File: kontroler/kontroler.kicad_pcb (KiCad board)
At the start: 2 copper layers, 147 x 78 mm, 44 parts, among them IC1 ATTINY841-SSU, P1 CONN_01X01, P2 CONN_01X01, P3 CONN_01X01, P4 CONN_01X01, P5 CONN_01X06, P6 CONN_01X06, P7 CONN_01X06, Q1 Q_PMOS_GDSD, Q2 Q_NPN_BEC, Q3 IRF8721PBF-1, Q4 Q_NMOS_GDSD, Q5 Q_NMOS_GDSD, Q6 Q_NMOS_GDSD, SW1 SW_PUSH, SW2 SW_PUSH, SW3 SW_PUSH, SW4 SW_PUSH, U1 LD1117S50CTR

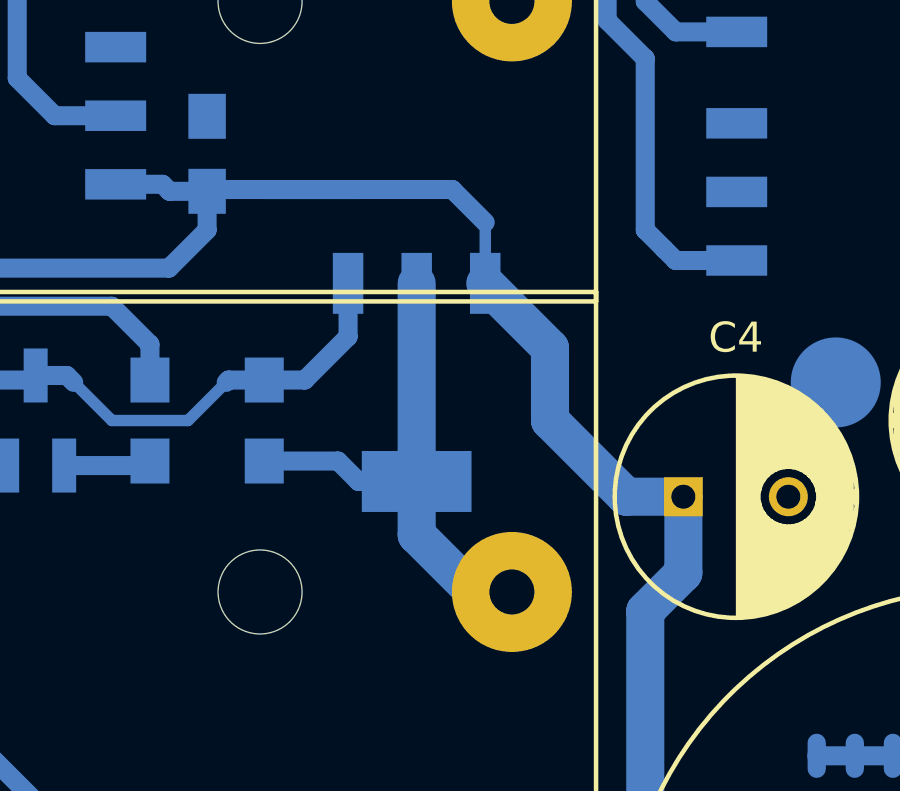
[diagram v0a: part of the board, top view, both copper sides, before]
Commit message: Fixed wrong p-mos orientation
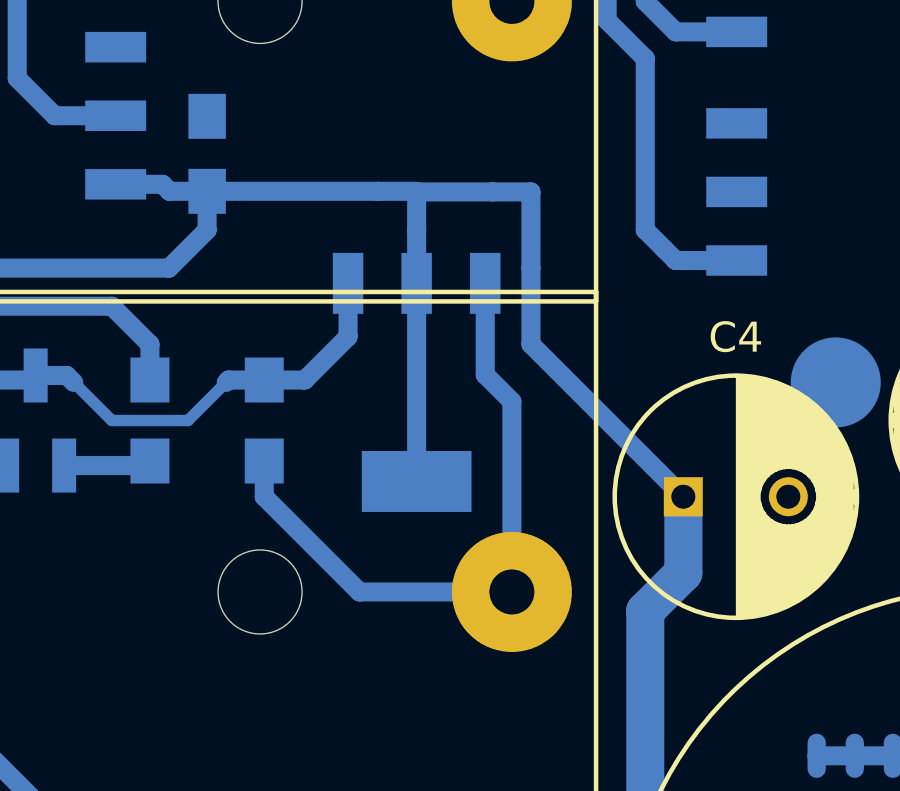
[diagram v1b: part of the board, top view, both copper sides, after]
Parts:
- R2: value R -> 33k
- R3: value R -> 12k
- R5: value R -> 47k
- R6: value R -> 3k3
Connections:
- Q1 pad 2: Net-(BT1-Pad1) -> Net-(C1-Pad1)
- Q1 pad 3: Net-(C1-Pad1) -> Net-(BT1-Pad1)
- Q1 pad 4: Net-(BT1-Pad1) -> Net-(C1-Pad1)
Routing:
- net Net-(BT1-Pad1): track 17.7 -> 22.7 mm
- net Net-(C1-Pad1): track 74.0 -> 69.1 mm

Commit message: Better layout
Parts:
- moved Q1 1.27 mm to (114.3, 74.9), turned to 180 degrees
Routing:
- net Net-(C1-Pad1): track 69.1 -> 58.2 mm
- net Net-(BT1-Pad1): track 22.7 -> 13.6 mm
- net Net-(D2-Pad2): track 18.2 -> 23.5 mm
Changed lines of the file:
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@@
   (general
     (links 94)
-    (no_connects 3)
+    (no_connects 4)
     (area 31.924999 39.924999 179.075001 118.075001)
     (thickness 1.6)
     (drawings 12)
-    (tracks 250)
+    (tracks 249)
     (zones 0)
     (modules 44)
@@
   )
   (module TO_SOT_Packages_SMD:SOT-223 (layer B.Cu)
-    (at 114.3 76.2)
+    (at 114.3 74.93 180)
     (descr "module CMS SOT223 4 pins")
     (tags "CMS SOT")
     (attr smd)
-    (fp_text reference Q1 (at 0 0.762) (layer B.SilkS)
-      (effects (font (size 1 1) (thickness 0.15)) (justify mirror))
-    )
-    (fp_text value Q_PMOS_GDSD (at 0 -0.762) (layer B.Fab)
+    (fp_text reference Q1 (at 0 0.762 180) (layer B.SilkS)
+      (effects (font (size 1 1) (thickness 0.15)) (justify mirror))
+    )
+    (fp_text value Q_PMOS_GDSD (at 0 -0.762 180) (layer B.Fab)
       (effects (font (size 1 1) (thickness 0.15)) (justify mirror))
     )
@@
     (fp_line (start 2.032 4.572) (end 3.556 2.286) (layer B.SilkS) (width 0.15))
     (fp_line (start 3.556 2.286) (end 3.556 1.524) (layer B.SilkS) (width 0.15))
-    (pad 4 smd rect (at 0 3.302) (size 3.6576 2.032) (layers B.Cu B.Paste B.Mask)
+    (pad 4 smd rect (at 0 3.302 180) (size 3.6576 2.032) (layers B.Cu B.Paste B.Mask)
       (net 4 "Net-(C1-Pad1)"))
-    (pad 2 smd rect (at 0 -3.302) (size 1.016 2.032) (layers B.Cu B.Paste B.Mask)
+    (pad 2 smd rect (at 0 -3.302 180) (size 1.016 2.032) (layers B.Cu B.Paste B.Mask)
       (net 4 "Net-(C1-Pad1)"))
-    (pad 3 smd rect (at 2.286 -3.302) (size 1.016 2.032) (layers B.Cu B.Paste B.Mask)
+    (pad 3 smd rect (at 2.286 -3.302 180) (size 1.016 2.032) (layers B.Cu B.Paste B.Mask)
       (net 1 "Net-(BT1-Pad1)"))
-    (pad 1 smd rect (at -2.286 -3.302) (size 1.016 2.032) (layers B.Cu B.Paste B.Mask)
+    (pad 1 smd rect (at -2.286 -3.302 180) (size 1.016 2.032) (layers B.Cu B.Paste B.Mask)
       (net 10 "Net-(D2-Pad2)"))
     (model TO_SOT_Packages_SMD.3dshapes/SOT-223.wrl
@@
   (gr_line (start 156 118) (end 156 40) (angle 90) (layer Edge.Cuts) (width 0.15))
   (gr_line (start 32 118) (end 156 118) (angle 90) (layer Edge.Cuts) (width 0.15))
-  (segment (start 117.475 83.185) (end 117.475 76.835) (width 0.635) (layer B.Cu) (net 1) (status 400000))
-  (segment (start 116.586 75.946) (end 116.586 72.898) (width 0.635) (layer B.Cu) (net 1) (status 800000))
-  (segment (start 117.475 76.835) (end 116.586 75.946) (width 0.635) (layer B.Cu) (net 1))
-  (segment (start 109.22 78.82) (end 109.22 80.01) (width 0.635) (layer B.Cu) (net 1))
-  (segment (start 112.395 83.185) (end 117.475 83.185) (width 0.635) (layer B.Cu) (net 1))
-  (segment (start 109.22 80.01) (end 112.395 83.185) (width 0.635) (layer B.Cu) (net 1))
+  (segment (start 109.22 78.82) (end 112.014 78.82) (width 0.635) (layer B.Cu) (net 1) (status C00000))
+  (segment (start 112.014 78.82) (end 111.934 78.74) (width 0.635) (layer B.Cu) (net 1) (status C00000))
+  (segment (start 111.934 78.74) (end 111.76 78.74) (width 0.635) (layer B.Cu) (net 1) (status C00000))
+  (segment (start 111.76 78.74) (end 112.014 78.232) (width 0.635) (layer B.Cu) (net 1) (status C00000))
+  (segment (start 117.475 83.185) (end 114.935 83.185) (width 1.27) (layer B.Cu) (net 1) (status 400000))
+  (segment (start 112.014 80.264) (end 112.014 78.232) (width 1.27) (layer B.Cu) (net 1) (status 800000))
+  (segment (start 114.935 83.185) (end 112.014 80.264) (width 1.27) (layer B.Cu) (net 1))
   (segment (start 117.475 83.185) (end 116.205 83.185) (width 1.27) (layer B.Cu) (net 1))
   (segment (start 45.085 83.185) (end 45.085 63.5) (width 2.54) (layer B.Cu) (net 2))
@@
   (segment (start 118.11 97.155) (end 118.11 104.14) (width 0.635) (layer F.Cu) (net 3))
   (via (at 118.11 97.155) (size 1.5) (drill 0.7) (layers F.Cu B.Cu) (net 3))
-  (segment (start 114.3 69.85) (end 116.84 69.85) (width 0.635) (layer B.Cu) (net 4))
-  (segment (start 118.11 74.93) (end 123.19 80.01) (width 0.635) (layer B.Cu) (net 4) (status 800000))
-  (segment (start 118.11 72.39) (end 118.11 74.93) (width 0.635) (layer B.Cu) (net 4))
-  (segment (start 118.11 69.85) (end 118.11 72.39) (width 0.635) (layer B.Cu) (net 4))
-  (segment (start 116.84 69.85) (end 118.11 69.85) (width 0.635) (layer B.Cu) (net 4))
-  (segment (start 114.3 71.12) (end 114.3 69.85) (width 0.635) (layer B.Cu) (net 4))
-  (segment (start 114.3 72.898) (end 114.3 71.12) (width 0.635) (layer B.Cu) (net 4) (status 400000))
-  (segment (start 114.28 69.83) (end 113.03 69.83) (width 0.635) (layer B.Cu) (net 4))
-  (segment (start 114.3 69.85) (end 114.28 69.83) (width 0.635) (layer B.Cu) (net 4))
-  (segment (start 107.315 69.83) (end 113.03 69.83) (width 0.635) (layer B.Cu) (net 4) (status 400000))
+  (segment (start 114.3 71.628) (end 117.348 71.628) (width 1.27) (layer B.Cu) (net 4) (status 400000))
+  (segment (start 119.38 76.2) (end 123.19 80.01) (width 1.27) (layer B.Cu) (net 4) (status 800000))
+  (segment (start 119.38 73.66) (end 119.38 76.2) (width 1.27) (layer B.Cu) (net 4))
+  (segment (start 117.348 71.628) (end 119.38 73.66) (width 1.27) (layer B.Cu) (net 4))
+  (segment (start 113.03 69.83) (end 113.03 69.85) (width 0.635) (layer B.Cu) (net 4))
+  (segment (start 113.03 69.85) (end 114.3 71.12) (width 0.635) (layer B.Cu) (net 4) (status 800000))
+  (segment (start 114.3 71.12) (end 114.3 71.628) (width 0.635) (layer B.Cu) (net 4) (status C00000))
+  (segment (start 107.315 69.83) (end 113.03 69.83) (width 0.635) (layer B.Cu) (net 4))
   (segment (start 113.03 69.83) (end 113.01 69.83) (width 0.635) (layer B.Cu) (net 4))
-  (segment (start 114.3 79.502) (end 114.3 72.898) (width 0.635) (layer B.Cu) (net 4))
   (segment (start 107.375 69.77) (end 107.315 69.83) (width 0.635) (layer B.Cu) (net 4))
   (segment (start 106.045 72.39) (end 93.345 72.39) (width 0.635) (layer B.Cu) (net 4))
@@
   (segment (start 93.345 72.39) (end 92.394594 71.439594) (width 0.635) (layer B.Cu) (net 4))
   (segment (start 121.92 95.25) (end 121.92 83.82) (width 1.27) (layer B.Cu) (net 4))
+  (segment (start 121.92 83.82) (end 123.19 82.55) (width 1.27) (layer B.Cu) (net 4))
   (segment (start 123.19 82.55) (end 123.19 80.01) (width 1.27) (layer B.Cu) (net 4))
-  (segment (start 121.92 83.82) (end 123.19 82.55) (width 1.27) (layer B.Cu) (net 4))
   (segment (start 107.335 69.85) (end 107.315 69.83) (width 0.381) (layer B.Cu) (net 4))
   (segment (start 107.315 69.83) (end 106.065 69.83) (width 0.635) (layer B.Cu) (net 4))
@@
   (segment (start 84.836 71.882) (end 87.122 71.882) (width 0.381) (layer B.Cu) (net 9))
   (segment (start 84.709 71.755) (end 84.836 71.882) (width 0.381) (layer B.Cu) (net 9))
-  (segment (start 112.014 72.898) (end 112.014 74.676) (width 0.635) (layer B.Cu) (net 10))
-  (segment (start 110.57 76.12) (end 109.22 76.12) (width 0.635) (layer B.Cu) (net 10))
-  (segment (start 112.014 74.676) (end 110.57 76.12) (width 0.635) (layer B.Cu) (net 10))
+  (segment (start 109.22 76.12) (end 109.3 76.12) (width 0.635) (layer B.Cu) (net 10) (status C00000))
+  (segment (start 109.3 76.12) (end 110.49 74.93) (width 0.635) (layer B.Cu) (net 10) (status 400000))
+  (segment (start 116.586 75.946) (end 116.586 78.232) (width 0.635) (layer B.Cu) (net 10) (status 800000))
+  (segment (start 115.57 74.93) (end 116.586 75.946) (width 0.635) (layer B.Cu) (net 10))
+  (segment (start 110.49 74.93) (end 115.57 74.93) (width 0.635) (layer B.Cu) (net 10))
+  (segment (start 109.22 76.12) (end 108.03 76.12) (width 0.635) (layer B.Cu) (net 10) (status 400000))
+  (segment (start 104.14 77.47) (end 102.87 76.2) (width 0.381) (layer B.Cu) (net 10))
+  (segment (start 106.68 77.47) (end 104.14 77.47) (width 0.381) (layer B.Cu) (net 10))
+  (segment (start 102.63886 75.96886) (end 102.87 76.2) (width 0.635) (layer B.Cu) (net 10))
+  (segment (start 102.63886 75.96886) (end 101.6 75.96886) (width 0.635) (layer B.Cu) (net 10))
   (segment (start 108.03 76.12) (end 106.68 77.47) (width 0.381) (layer B.Cu) (net 10))
-  (segment (start 109.22 76.12) (end 108.03 76.12) (width 0.635) (layer B.Cu) (net 10))
-  (segment (start 108.03 76.12) (end 107.95 76.2) (width 0.635) (layer B.Cu) (net 10))
   (segment (start 97.79 76.12) (end 101.44886 76.12) (width 0.635) (layer B.Cu) (net 10))
   (segment (start 101.44886 76.12) (end 101.6 75.96886) (width 0.635) (layer B.Cu) (net 10))
-  (segment (start 101.6 75.96886) (end 102.63886 75.96886) (width 0.635) (layer B.Cu) (net 10))
-  (segment (start 102.63886 75.96886) (end 102.87 76.2) (width 0.635) (layer B.Cu) (net 10))
-  (segment (start 106.68 77.47) (end 104.14 77.47) (width 0.381) (layer B.Cu) (net 10))
-  (segment (start 104.14 77.47) (end 102.87 76.2) (width 0.381) (layer B.Cu) (net 10))
   (segment (start 101.6 76.2) (end 101.6 75.96886) (width 0.381) (layer B.Cu) (net 10))
   (segment (start 128.905 94.234) (end 127.635 94.234) (width 1.27) (layer B.Cu) (net 11))
